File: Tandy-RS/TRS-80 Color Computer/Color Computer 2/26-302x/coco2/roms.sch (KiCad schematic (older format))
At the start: 4 parts, among them U12 MC68A364, U13 MC68A364

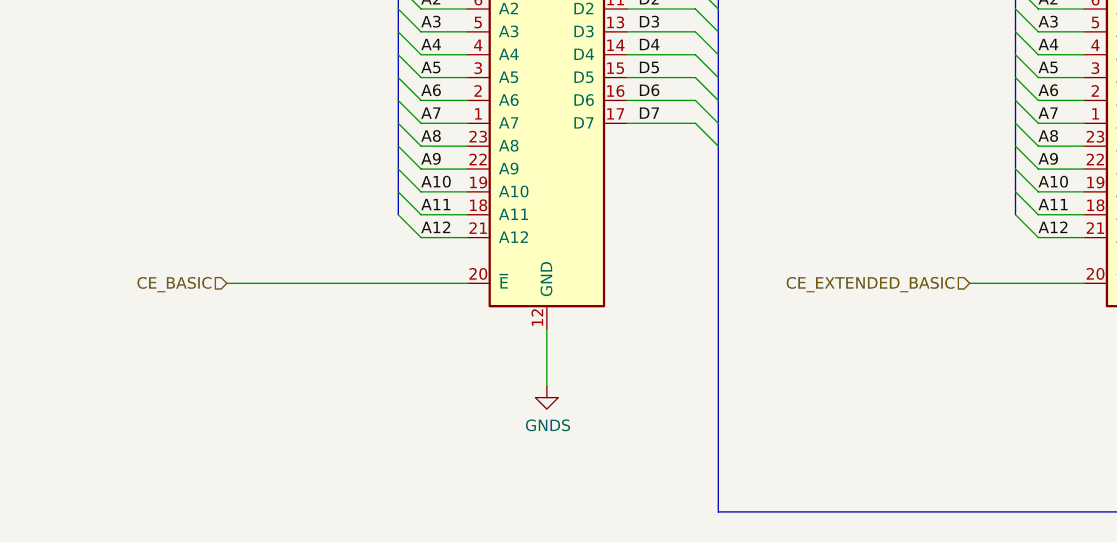
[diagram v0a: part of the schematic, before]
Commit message: -Finished SAM sheet -Finsihed DRAM sheet
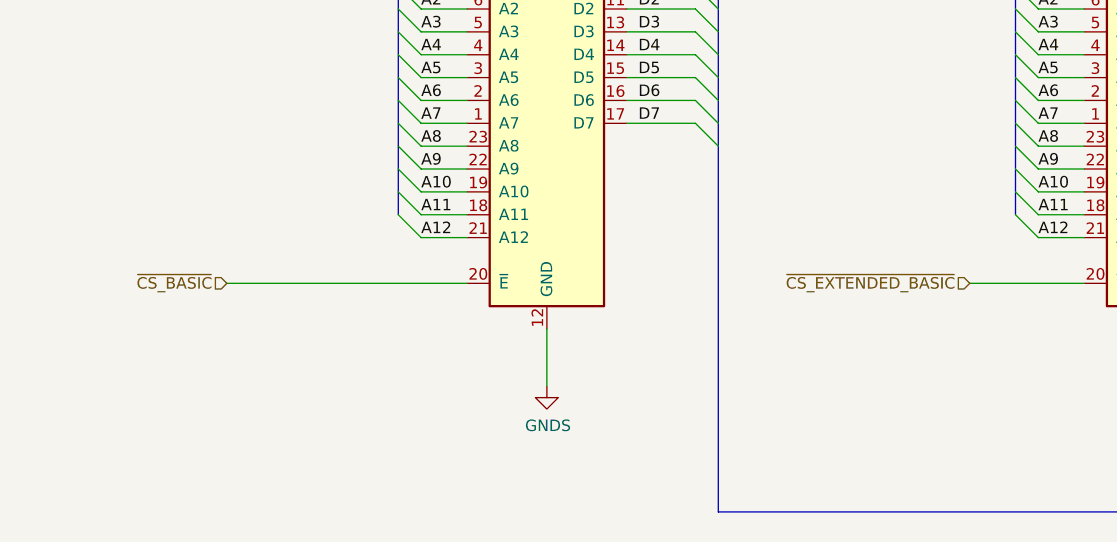
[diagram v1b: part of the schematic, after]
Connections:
- net CE_BASIC renamed ~CS_BASIC
- net CE_EXTENDED_BASIC renamed ~CS_EXTENDED_BASIC
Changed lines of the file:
@@
 	3900 4550 2850 4550
 Text HLabel 2850 4550 0    50   Input ~ 0
-CE_BASIC
+~CS_BASIC
 Text HLabel 6100 4550 0    50   Input ~ 0
-CE_EXTENDED_BASIC
+~CS_EXTENDED_BASIC
 Wire Wire Line
 	6100 4550 6600 4550

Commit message: -Finished PCB border -Placed components to match original board -added some 3D models for some components
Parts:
- U12, U13: footprint Package_DIP:DIP-24_W15.24mm_Socket_LongPads -> Package_DIP:DIP-24_W15.24mm_Socket
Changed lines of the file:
@@
 F 0 "U12" H 4150 4950 50  0000 C CNN
 F 1 "MC68A364" H 4050 4850 50  0000 C CNN
-F 2 "Package_DIP:DIP-24_W15.24mm_Socket_LongPads" H 5550 5550 50  0001 C CNN
+F 2 "Package_DIP:DIP-24_W15.24mm_Socket" H 5550 5550 50  0001 C CNN
 F 3 "" H 5550 5550 50  0001 C CNN
 	1    4250 3850
@@
 F 0 "U13" H 6850 4900 50  0000 C CNN
 F 1 "MC68A364" H 6750 4800 50  0000 C CNN
-F 2 "Package_DIP:DIP-24_W15.24mm_Socket_LongPads" H 8250 5550 50  0001 C CNN
+F 2 "Package_DIP:DIP-24_W15.24mm_Socket" H 8250 5550 50  0001 C CNN
 F 3 "" H 8250 5550 50  0001 C CNN
 	1    6950 3850

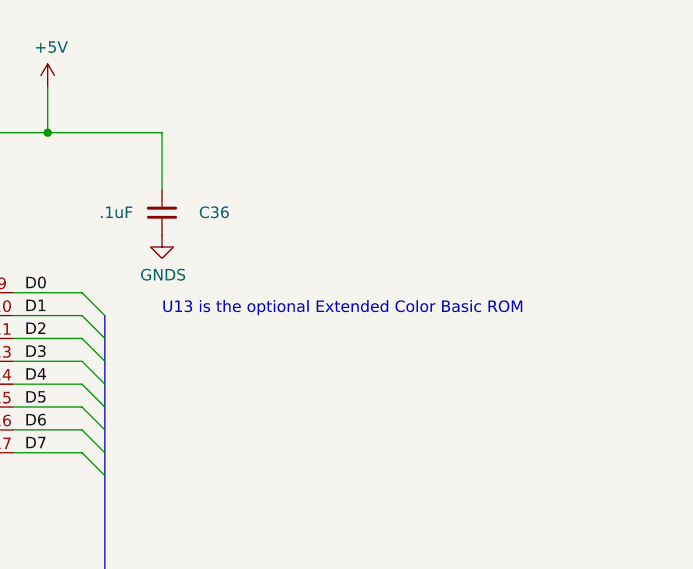
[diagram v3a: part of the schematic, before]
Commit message: -Finished PCB -Verified componenents that could be bought. -Added relay in parallel with discontinued relay
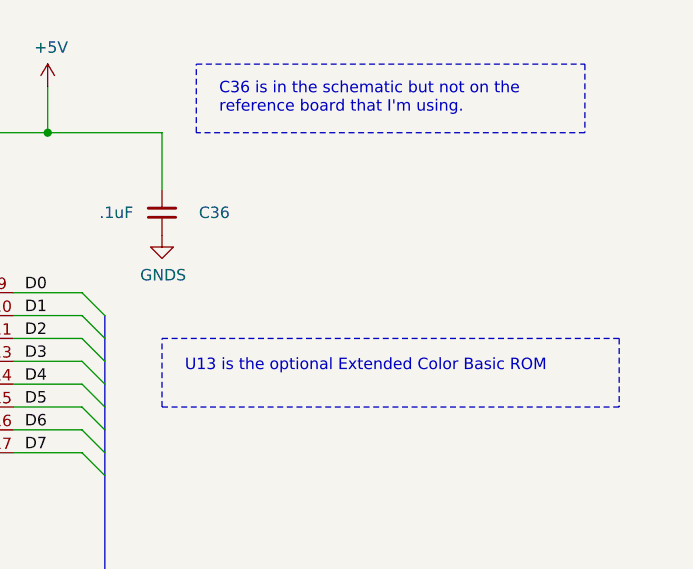
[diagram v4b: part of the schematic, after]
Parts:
- C35, C36: Field4 digikey -> (none); Field5 1109PHTR-ND -> (none); Manufacturer part# (none) -> A104K15X7RF5TAA; Vendor (none) -> digikey; Vendor part# (none) -> 1109PHCT-ND
- U12, U13: Manufacturer part# (none) -> 243-24-1-06; Vendor (none) -> digikey; Vendor part# (none) -> 1175-2551-ND
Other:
- note added: "C36 is in the schematic but not on the \nreference board that I'm using.\n\n"
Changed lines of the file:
@@
 F 1 "MC68A364" H 4050 4850 50  0000 C CNN
 F 2 "Package_DIP:DIP-24_W15.24mm_Socket" H 5550 5550 50  0001 C CNN
-F 3 "" H 5550 5550 50  0001 C CNN
+F 3 "http://www.cnctech.us/pdfs/243-XX-1-XX_.pdf" H 5550 5550 50  0001 C CNN
+F 4 "digikey" H 4250 3850 50  0001 C CNN "Vendor"
+F 5 "1175-2551-ND" H 4250 3850 50  0001 C CNN "Vendor part#"
+F 6 "243-24-1-06" H 4250 3850 50  0001 C CNN "Manufacturer part#"
 	1    4250 3850
 	1    0    0    -1
@@
 F 1 "MC68A364" H 6750 4800 50  0000 C CNN
 F 2 "Package_DIP:DIP-24_W15.24mm_Socket" H 8250 5550 50  0001 C CNN
-F 3 "" H 8250 5550 50  0001 C CNN
+F 3 "http://www.cnctech.us/pdfs/243-XX-1-XX_.pdf" H 8250 5550 50  0001 C CNN
+F 4 "digikey" H 6950 3850 50  0001 C CNN "Vendor"
+F 5 "1175-2551-ND" H 6950 3850 50  0001 C CNN "Vendor part#"
+F 6 "243-24-1-06" H 6950 3850 50  0001 C CNN "Manufacturer part#"
 	1    6950 3850
 	1    0    0    -1
@@
 F 2 "Capacitor_THT:C_Axial_L3.8mm_D2.6mm_P10.00mm_Horizontal" H 5250 2850 50  0001 C CNN
 F 3 "https://www.vishay.com/docs/45164/aseries.pdf" H 5250 2850 50  0001 C CNN
-F 4 "digikey" V 5250 2850 50  0001 C CNN "Field4"
-F 5 "1109PHTR-ND" V 5250 2850 50  0001 C CNN "Field5"
+F 4 "digikey" V 5250 2850 50  0001 C CNN "Vendor"
+F 5 "1109PHCT-ND" V 5250 2850 50  0001 C CNN "Vendor part#"
+F 6 "A104K15X7RF5TAA" H 5250 2850 50  0001 C CNN "Manufacturer part#"
 	1    5250 2850
 	-1   0    0    1
@@
 F 2 "Capacitor_THT:C_Axial_L3.8mm_D2.6mm_P10.00mm_Horizontal" H 7950 2800 50  0001 C CNN
 F 3 "https://www.vishay.com/docs/45164/aseries.pdf" H 7950 2800 50  0001 C CNN
-F 4 "digikey" V 7950 2800 50  0001 C CNN "Field4"
-F 5 "1109PHTR-ND" V 7950 2800 50  0001 C CNN "Field5"
+F 4 "digikey" V 7950 2800 50  0001 C CNN "Vendor"
+F 5 "1109PHCT-ND" V 7950 2800 50  0001 C CNN "Vendor part#"
+F 6 "A104K15X7RF5TAA" H 7950 2800 50  0001 C CNN "Manufacturer part#"
 	1    7950 2800
 	-1   0    0    1
@@
 Text Notes 2300 3250 0    50   ~ 0
 U12 is the Color Basic ROM.
-Text Notes 7950 3250 0    50   ~ 0
+Text Notes 8050 3500 0    50   ~ 0
 U13 is the optional Extended Color Basic ROM
 $Comp
@@
 Text Label 3700 4350 0    50   ~ 0
 A12
+Text Notes 8200 2450 0    50   ~ 0
+C36 is in the schematic but not on the \nreference board that I'm using.\n\n
+Wire Notes Line
+	9800 2150 9800 2450
+Wire Notes Line
+	9800 2450 8100 2450
+Wire Notes Line
+	8100 2450 8100 2150
+Wire Notes Line
+	8100 2150 9800 2150
+Wire Notes Line
+	9950 3350 9950 3650
+Wire Notes Line
+	9950 3650 7950 3650
+Wire Notes Line
+	7950 3650 7950 3350
+Wire Notes Line
+	7950 3350 9950 3350
 Wire Bus Line
 	5000 3250 5000 5550
